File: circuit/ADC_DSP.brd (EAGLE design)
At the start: 80 x 80 mm, 82 parts, among them IC1 REG1117, IC2 74HC4052D, IC3 STM32F40XRXT6, IC4 CS4272, Q1 8MHz, Q2 24.576MHz

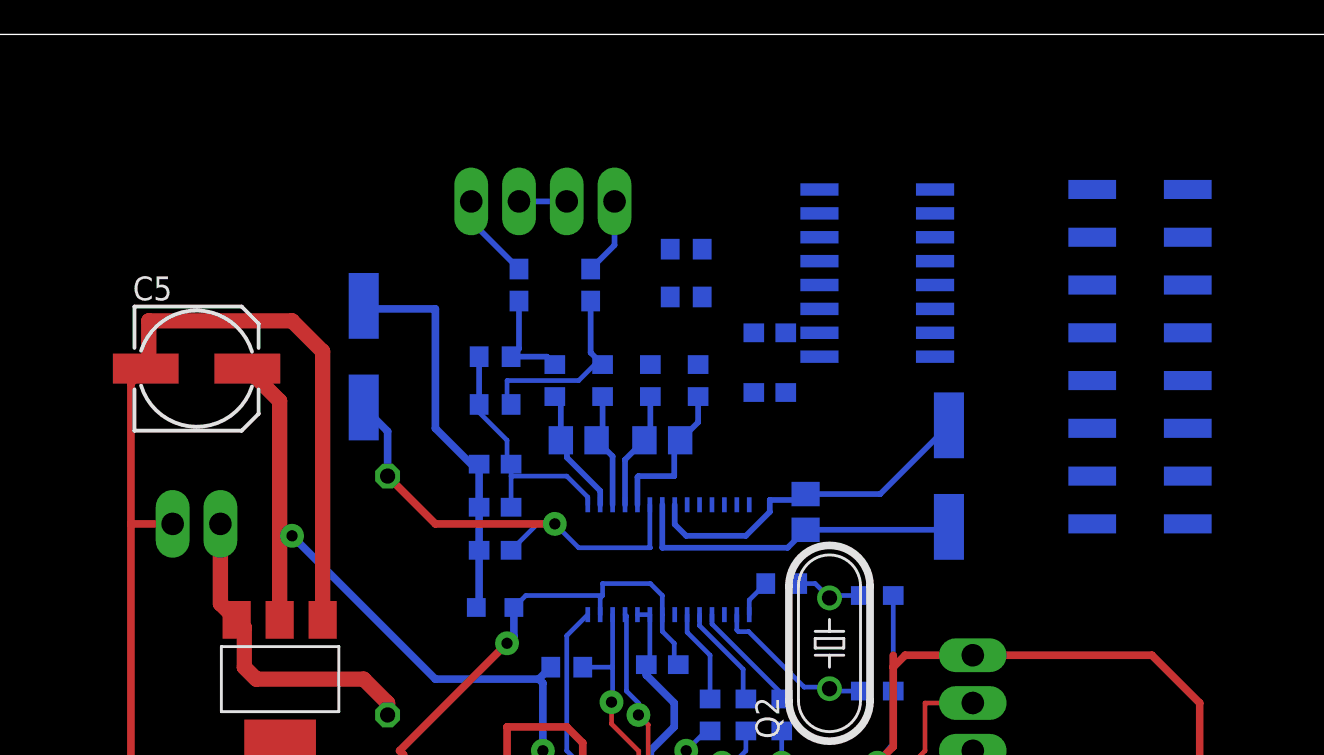
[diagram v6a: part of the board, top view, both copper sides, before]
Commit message: - перержавел по халявному под SN74LVC1G3157DBVR
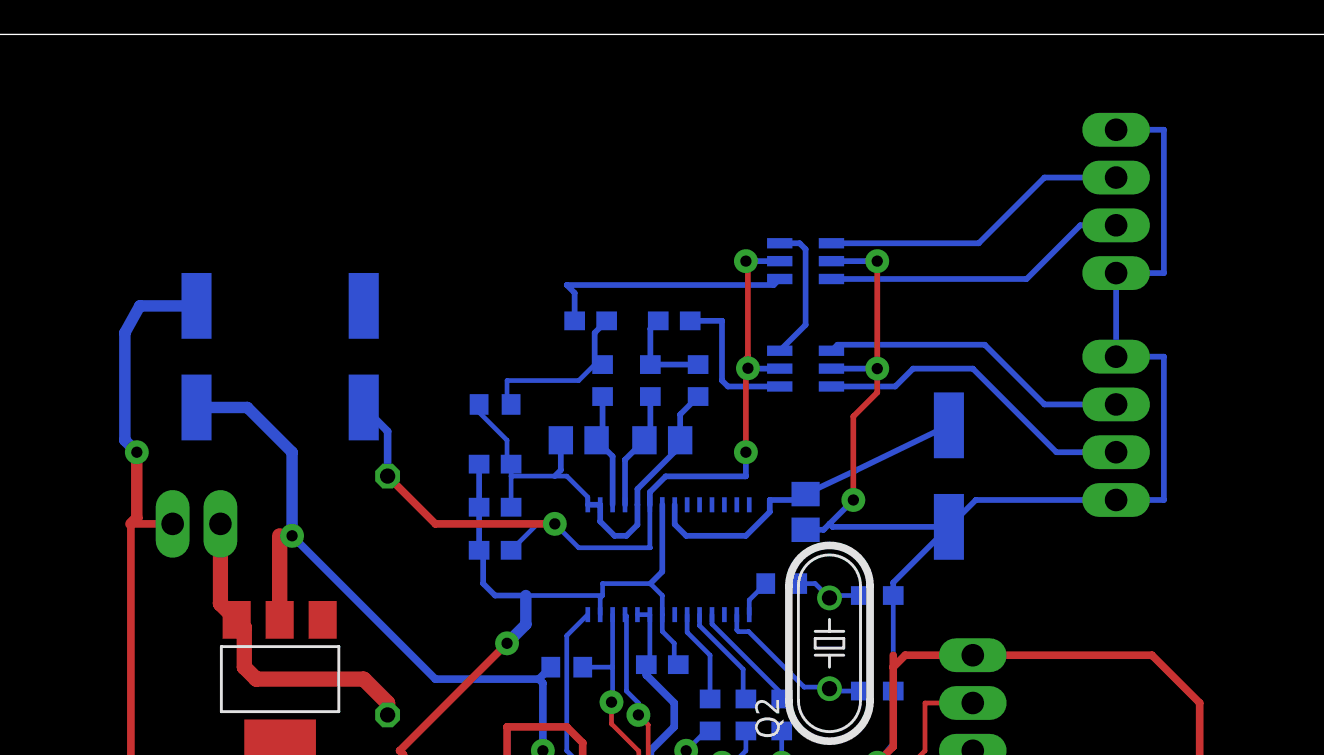
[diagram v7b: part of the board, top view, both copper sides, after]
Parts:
- removed C13, C36: 2.2u, rcl:C0603
- removed IC2: 74HC4052D, 40xx:SO16
- removed INA: (no value), con-phoenix-254:4POL254
- removed INB: PIN8X2, balmer:PIN8X2_SMD
- removed L3: (no value), rcl:L2012C
- removed R27, R30: 1.2k, rcl:R0603
- removed R31, R33: 10k, rcl:R0603
- added U$1, U$2: SN74LVC1G3157DBVR, balmer:SOT23-6
- added X1, X2: (no value), con-phoenix-254:4POL254
- C20: value 2.2u -> 1u
- moved C25 6.35 mm to (36.8, 64.8)
- moved R34 4.49 mm to (38.1, 61.6), turned to 90 degrees
- moved C35 1.91 mm to (32.4, 64.8), turned to 0 degrees
- moved C5 0.64 mm to (11.4, 62.9), flipped to the bottom, turned to 270 degrees
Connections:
- removed net 4052_A: C3.1, GPIO.1, IC2.10, R23.1
- removed net AGND: C1.-, C20.2, C22.2, C24.2, C26.2, C8.-, IC2.6, IC2.7, IC2.8, IC4.21, INA.2, INA.3, INB.P$10, INB.P$12, INB.P$14, INB.P$16, INB.P$2, INB.P$4, INB.P$6, INB.P$8, L3.2
- removed net N$42: IC2.5, INB.P$11
- removed net N$43: IC2.1, INB.P$9
- removed net N$44: IC2.11, INB.P$7
- removed net N$45: IC2.15, INB.P$5
- removed net N$46: IC2.14, INB.P$3
- removed net N$47: IC2.12, INB.P$1
- removed net N$48: C28.2, IC4.16, R30.1
- removed net N$51: C36.1, R30.2, R31.2
- removed net N$59: C35.2, INA.1
- removed net N$60: C36.2, INA.4
- new net SW_A: C3.1, GPIO.1, R23.1, U$1.6, U$2.6
- net 4052_B: no longer IC2.9
- net AVCC: now also U$1.5, U$2.5; no longer IC2.16
- net GND: now also C1.-, C20.2, C22.2, C24.2, C26.2, C8.-, IC4.21, U$1.2, U$2.2, X1.1, X1.4, X2.1, X2.4; no longer L3.1
- net N$13: now also U$1.4; no longer IC2.3
- net N$15: now also C35.2, U$2.4; no longer C27.1, IC4.19, R27.1
- net N$26: now also U$1.3, X1.2; no longer IC2.4, INB.P$15
- net N$28: now also U$1.1, X1.3; no longer C13.1, R27.2, R33.2
- net N$30: now also U$2.3, X2.2; no longer C13.2, IC2.13
- net N$38: now also U$2.1, X2.3; no longer IC2.2, INB.P$13
- net VCOM: now also C27.1, C28.2, IC4.16, IC4.19; no longer R31.1, R33.1
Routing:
- net GND: track 376.5 -> 441.6 mm, vias 7 -> 11
- net AGND: track 41.6 -> 0.00 mm
- net AVCC: track 24.9 -> 46.7 mm, vias 1 -> 4
- net N$26: track 0.00 -> 17.4 mm
- net N$38: track 0.00 -> 16.6 mm
- net N$28: track 0.00 -> 16.6 mm
- net N$30: track 0.00 -> 16.3 mm
- net SW_A: track 0.00 -> 13.9 mm
- net VCOM: track 13.7 -> 25.4 mm
- net N$13: track 0.00 -> 8.07 mm
- net N$48: track 6.75 -> 0.00 mm
- net 4052_A: track 6.46 -> 0.00 mm
- net N$51: track 5.63 -> 0.00 mm
- net N$15: track 8.21 -> 13.5 mm
- net N$39: track 0.00 -> 5.04 mm
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
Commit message: - более -менее разведенная плата
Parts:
- removed X2: (no value), con-phoenix-254:4POL254
- added C13: 100n, rcl:C0603
- X1: device con-phoenix-254:4POL254 -> con-phoenix-254:8POL254
- moved X1 32.7 mm to (30.5, 72.4), turned to 0 degrees
- moved U$2 19.2 mm to (24.8, 65.4), turned to 180 degrees
- moved C35 10.5 mm to (22.9, 60.3), turned to 90 degrees
- moved U$1 8.25 mm to (36.2, 65.4), turned to 180 degrees
- moved C1 5.24 mm to (46.4, 55.2)
- moved R12 5.24 mm to (55.2, 34.9)
- moved C10 5.24 mm to (41.7, 35.6)
- moved R13 5.24 mm to (55.2, 30.2)
- moved R15 5.24 mm to (34.8, 16.0)
- moved R20 5.24 mm to (55.2, 22.2)
- moved R21 5.24 mm to (55.2, 14.6)
- moved R3 5.24 mm to (55.2, 32.5)
- moved R4 5.24 mm to (55.2, 9.53)
- moved R5 5.24 mm to (55.2, 19.7)
- moved R6 5.24 mm to (55.2, 24.8)
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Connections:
- net AVCC: now also C13.1
- net GND: now also C13.2, X1.5, X1.8; no longer X2.1, X2.4
- net N$30: now also X1.6; no longer X2.2
- net N$38: now also X1.7; no longer X2.3
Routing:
- net GND: track 441.6 -> 470.6 mm, vias 11 -> 10
- net SW_A: track 13.9 -> 26.0 mm, vias 0 -> 4
- net N$26: track 17.4 -> 5.80 mm, vias 0 -> 1
- net N$38: track 16.6 -> 5.80 mm, vias 0 -> 1
- net N$28: track 16.6 -> 6.01 mm, vias 0 -> 1
- net N$30: track 16.3 -> 6.01 mm, vias 0 -> 1
- net AVCC: track 46.7 -> 55.6 mm, vias 4 -> 0
- net N$15: track 13.5 -> 5.05 mm
- net +3V3: track 188.7 -> 183.4 mm
- net N$13: track 8.07 -> 3.64 mm
- net N$50: track 9.38 -> 6.16 mm
- net VCOM: track 25.4 -> 24.0 mm
- net N$39: track 5.04 -> 5.78 mm
- net PB8(AU_RST): track 13.4 -> 12.8 mm
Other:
- board size 80 x 80 mm -> 64.8 x 76.8 mm
